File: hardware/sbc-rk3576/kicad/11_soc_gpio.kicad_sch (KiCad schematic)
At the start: 1 part, among them U401 RK3576

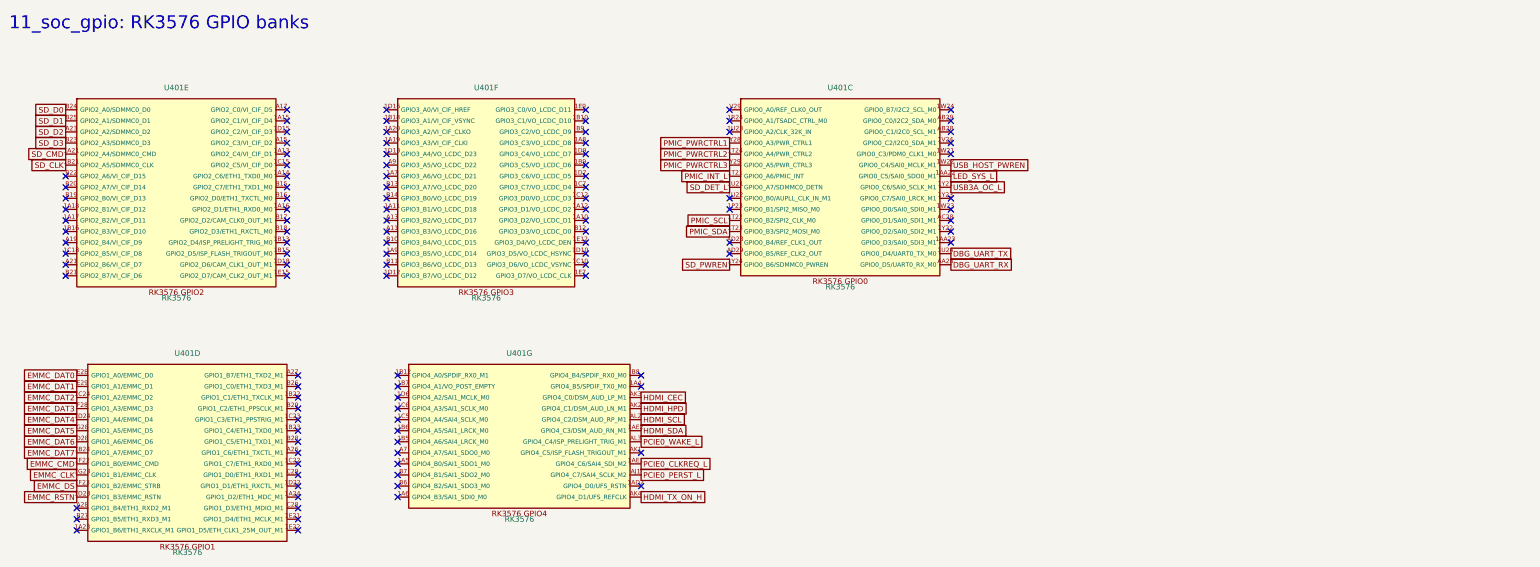
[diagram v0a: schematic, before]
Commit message: hardware: add GbE, USB hub + 2x USB-A, Wi-Fi5/BT; real RK3576 land pattern; 100x72 board
- RK3576 footprint from LCSC C42388007 (all 698 ball IDs verified against the
  datasheet) replaces the placeholder.
- RTL8211F-CG RGMII PHY + HR911130C MagJack, FE1.1s 4-port hub (pinout per
  Terminus datasheet), stacked dual USB-A, BL-M8821CU1 Wi-Fi 5/BT 4.2 + u.FL.
- LCSC footprints get pad-derived courtyards; RJ45 pegs become NPTH.
- ERC 0/0, DRC 0 violations, parity 0 (placement stage).

Co-Authored-By: Claude Opus 5.5 <noreply@anthropic.com>
Claude-Session: https://claude.ai/code/session_01DP7VBm9fUdwhcDWq3gWKJ6
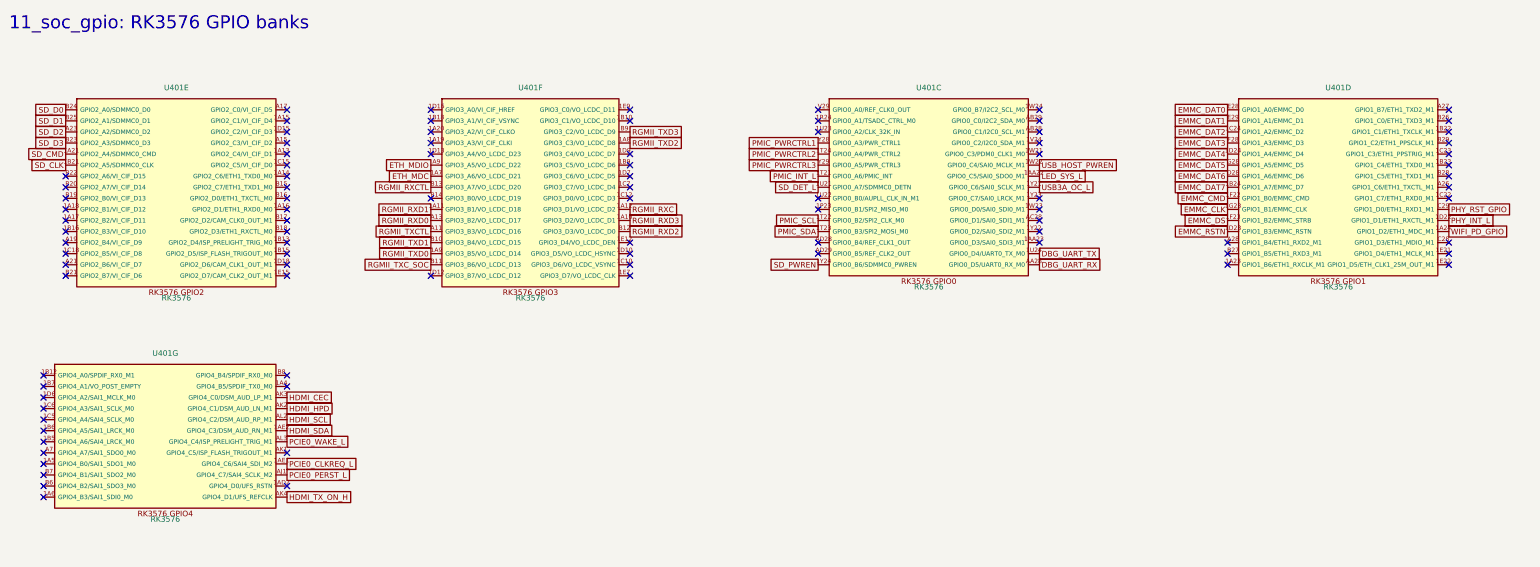
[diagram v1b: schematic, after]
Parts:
- U401: footprint sbc:RK3576_FCCSP-698_16.1x17.2mm_PLACEHOLDER -> sbc:RK3576_FCCSP-698_16.1x17.2mm
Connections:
- net RGMII_RXD3: now reaches U401.1A10 (GPIO3_D2/VO_LCDC_D1)
- net RGMII_RXD1: now reaches U401.1A11 (GPIO3_B1/VO_LCDC_D18)
- net RGMII_RXC: now reaches U401.1A12 (GPIO3_D1/VO_LCDC_D2)
- net ETH_MDC: now reaches U401.1A7 (GPIO3_A6/VO_LCDC_D21)
- net RGMII_TXD2: now reaches U401.1A8 (GPIO3_C3/VO_LCDC_D8)
- net RGMII_TXD0: now reaches U401.1A9 (GPIO3_B5/VO_LCDC_D14)
- net RGMII_TXCTL: now reaches U401.A11 (GPIO3_B3/VO_LCDC_D16)
- net RGMII_RXD0: now reaches U401.A13 (GPIO3_B2/VO_LCDC_D17)
- net ETH_MDIO: now reaches U401.A9 (GPIO3_A5/VO_LCDC_D22)
- net RGMII_TXD1: now reaches U401.B10 (GPIO3_B4/VO_LCDC_D15)
- net RGMII_TXC_SOC: now reaches U401.B11 (GPIO3_B6/VO_LCDC_D13)
- net RGMII_RXD2: now reaches U401.B12 (GPIO3_D3/VO_LCDC_D0)
- net RGMII_RXCTL: now reaches U401.B13 (GPIO3_A7/VO_LCDC_D20)
- net RGMII_TXD3: now reaches U401.B9 (GPIO3_C2/VO_LCDC_D9)
- net WIFI_PD_GPIO: now reaches U401.1A24 (GPIO1_D2/ETH1_MDC_M1)
- net PHY_INT_L: now reaches U401.1D22 (GPIO1_D1/ETH1_RXCTL_M1)
- net PHY_RST_GPIO: now reaches U401.C29 (GPIO1_D0/ETH1_RXD1_M1)
- no-connect marks 109 -> 92
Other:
- moved on the sheet: U401C, U401D, U401F, U401G
